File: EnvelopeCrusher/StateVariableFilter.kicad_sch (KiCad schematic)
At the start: 21 parts

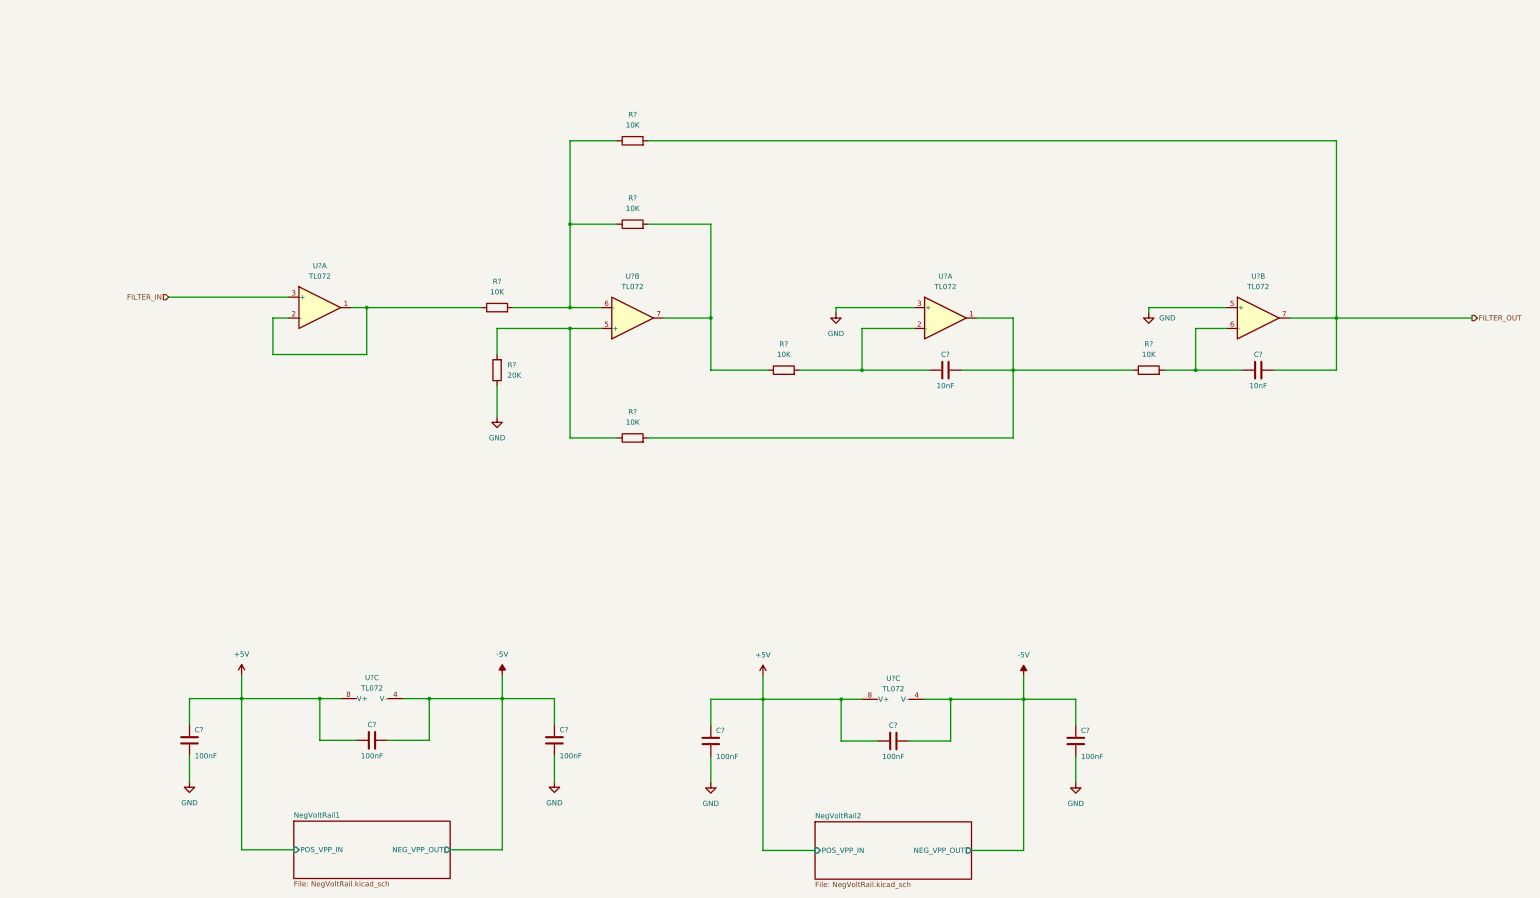
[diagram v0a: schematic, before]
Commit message: updated signal path
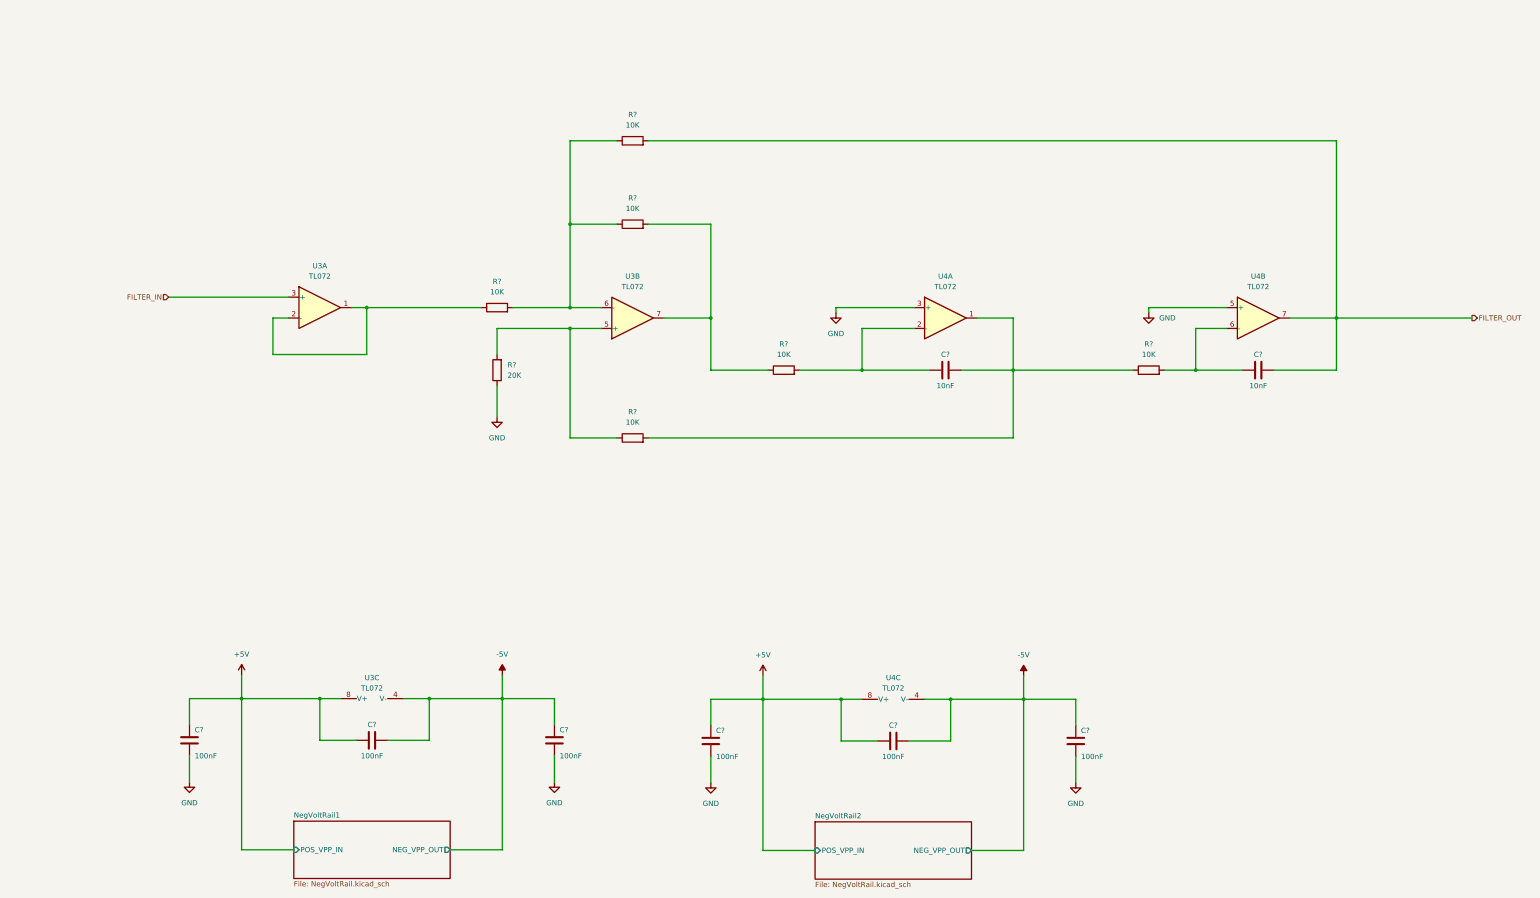
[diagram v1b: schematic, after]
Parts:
- gave numbers to parts that had none: 2
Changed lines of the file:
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@@
   (symbol (lib_id "Amplifier_Operational:TL072") (at 247.65 111.76 0) (unit 1)
     (in_bom yes) (on_board yes) (fields_autoplaced)
-    (property "Reference" "U?" (id 0) (at 247.65 101.6 0))
+    (property "Reference" "U4" (id 0) (at 247.65 101.6 0))
     (property "Value" "TL072" (id 1) (at 247.65 104.14 0))
     (property "Footprint" "" (id 2) (at 247.65 111.76 0)
@@
   (symbol (lib_id "Amplifier_Operational:TL072") (at 171.45 111.76 0) (mirror x) (unit 2)
     (in_bom yes) (on_board yes) (fields_autoplaced)
-    (property "Reference" "U?" (id 0) (at 171.45 101.6 0))
+    (property "Reference" "U3" (id 0) (at 171.45 101.6 0))
     (property "Value" "TL072" (id 1) (at 171.45 104.14 0))
     (property "Footprint" "" (id 2) (at 171.45 111.76 0)
@@
   (symbol (lib_id "Amplifier_Operational:TL072") (at 107.95 201.93 90) (unit 3)
     (in_bom yes) (on_board yes) (fields_autoplaced)
-    (property "Reference" "U?" (id 0) (at 107.95 199.39 90))
+    (property "Reference" "U3" (id 0) (at 107.95 199.39 90))
     (property "Value" "TL072" (id 1) (at 107.95 201.93 90))
     (property "Footprint" "" (id 2) (at 107.95 201.93 0)
@@
   (symbol (lib_id "Amplifier_Operational:TL072") (at 234.95 202.0941 90) (unit 3)
     (in_bom yes) (on_board yes) (fields_autoplaced)
-    (property "Reference" "U?" (id 0) (at 234.95 199.5541 90))
-    (property "Value" "TL072" (id 1) (at 234.95 202.0941 90))
+    (property "Reference" "U4" (id 0) (at 234.95 199.39 90))
+    (property "Value" "TL072" (id 1) (at 234.95 201.93 90))
     (property "Footprint" "" (id 2) (at 234.95 202.0941 0)
       (effects (font (size 1.27 1.27)) hide)
@@
   (symbol (lib_id "Amplifier_Operational:TL072") (at 95.25 109.22 0) (unit 1)
     (in_bom yes) (on_board yes) (fields_autoplaced)
-    (property "Reference" "U?" (id 0) (at 95.25 99.06 0))
+    (property "Reference" "U3" (id 0) (at 95.25 99.06 0))
     (property "Value" "TL072" (id 1) (at 95.25 101.6 0))
     (property "Footprint" "" (id 2) (at 95.25 109.22 0)
@@
   (symbol (lib_id "Amplifier_Operational:TL072") (at 323.85 111.76 0) (unit 2)
     (in_bom yes) (on_board yes) (fields_autoplaced)
-    (property "Reference" "U?" (id 0) (at 323.85 101.6 0))
+    (property "Reference" "U4" (id 0) (at 323.85 101.6 0))
     (property "Value" "TL072" (id 1) (at 323.85 104.14 0))
     (property "Footprint" "" (id 2) (at 323.85 111.76 0)

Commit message: Add routing
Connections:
- net SWEEP_3Y: now reaches C?.1, U4.2 (-)
- net SWEEP_3Y: no longer R?.2
- net SWEEP_4Y: now reaches C?.1, U4.6 (-)
- net SWEEP_4Y: no longer R?.2
- new net SWEEP_3Z: R?.2
- new net SWEEP_4Z: R?.2
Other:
- note added: "74HC4066 Analog Switch"
- moved on the sheet: C?, R?, U3A, U3B, U4A

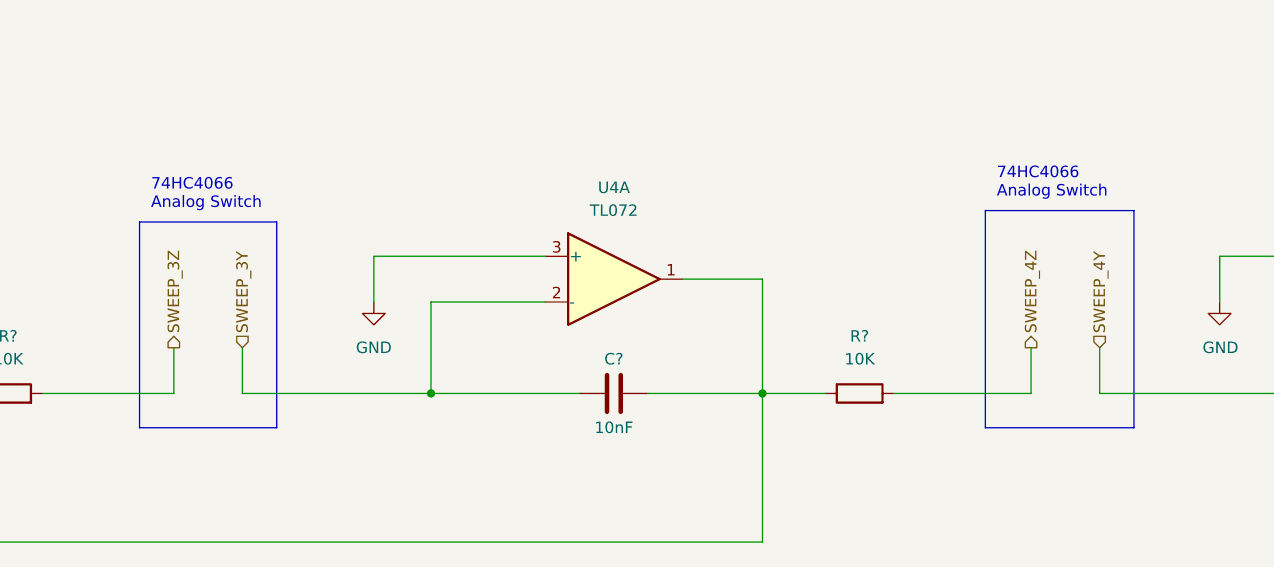
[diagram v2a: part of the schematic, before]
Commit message: REARRANGED BLOCK DIAGRAM AND ROUTING
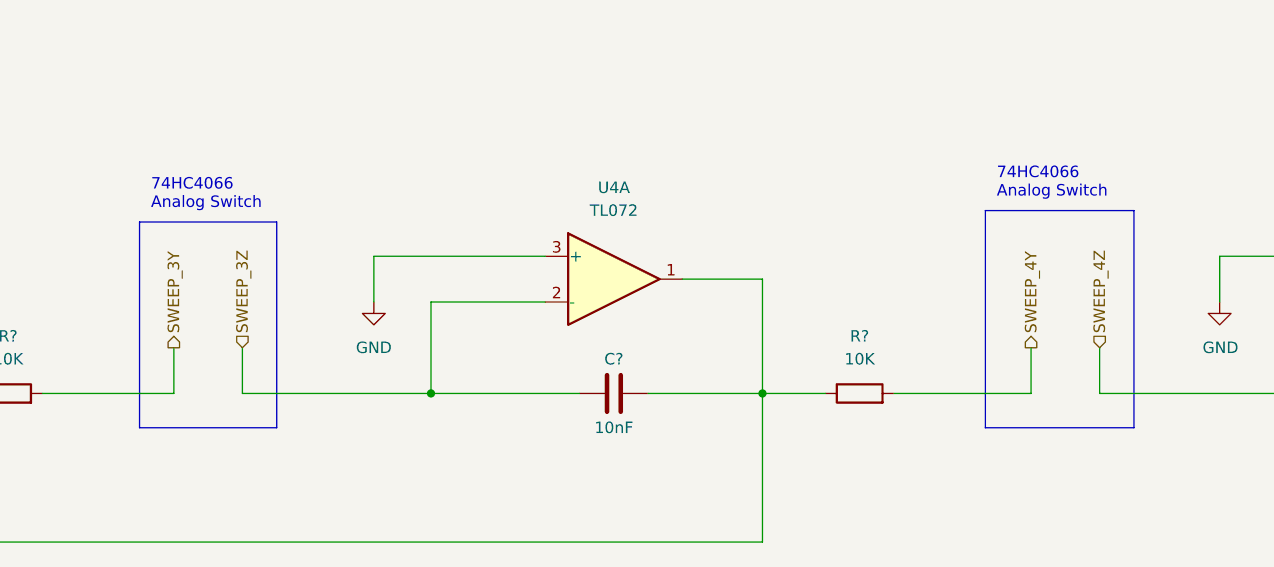
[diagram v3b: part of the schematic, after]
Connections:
- net SWEEP_3Y: now also R?.2; no longer C?.1, U4.2 (-)
- net SWEEP_3Z: now also C?.1, U4.2 (-); no longer R?.2
- net SWEEP_4Y: now also R?.2; no longer C?.1, U4.6 (-)
- net SWEEP_4Z: now also C?.1, U4.6 (-); no longer R?.2
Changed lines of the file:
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@@
     (effects (font (size 1.27 1.27)) (justify left))
   )
-  (hierarchical_label "SWEEP_4Z" (shape output) (at 279.4 119.38 90)
+  (hierarchical_label "SWEEP_4Z" (shape input) (at 287.02 119.38 90)
     (effects (font (size 1.27 1.27)) (justify left))
   )
-  (hierarchical_label "SWEEP_4Y" (shape input) (at 287.02 119.38 90)
+  (hierarchical_label "SWEEP_4Y" (shape output) (at 279.4 119.38 90)
     (effects (font (size 1.27 1.27)) (justify left))
   )
@@
     (effects (font (size 1.27 1.27)) (justify right))
   )
-  (hierarchical_label "SWEEP_3Y" (shape input) (at 191.77 119.38 90)
+  (hierarchical_label "SWEEP_3Y" (shape output) (at 184.15 119.38 90)
     (effects (font (size 1.27 1.27)) (justify left))
   )
-  (hierarchical_label "SWEEP_3Z" (shape output) (at 184.15 119.38 90)
+  (hierarchical_label "SWEEP_3Z" (shape input) (at 191.77 119.38 90)
     (effects (font (size 1.27 1.27)) (justify left))
   )

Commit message: Completed Schematic
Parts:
- gave numbers to parts that had none: 15
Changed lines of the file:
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@@
+    (stroke (width 0) (type default) (color 0 0 0 0))
+  )
+  (wire (pts (xy 121.92 198.12) (xy 121.92 204.47))
     (stroke (width 0) (type default) (color 0 0 0 0))
   )
@@
   (symbol (lib_id "power:GND") (at 300.355 114.3 0) (unit 1)
     (in_bom yes) (on_board yes)
-    (property "Reference" "#PWR?" (id 0) (at 300.355 120.65 0)
+    (property "Reference" "#PWR030" (id 0) (at 300.355 120.65 0)
       (effects (font (size 1.27 1.27)) hide)
     )
@@
   (symbol (lib_id "power:+5V") (at 76.2 198.7479 0) (unit 1)
     (in_bom yes) (on_board yes) (fields_autoplaced)
-    (property "Reference" "#PWR?" (id 0) (at 76.2 202.5579 0)
+    (property "Reference" "#PWR021" (id 0) (at 76.2 202.5579 0)
       (effects (font (size 1.27 1.27)) hide)
     )
@@
   (symbol (lib_id "Device:R") (at 104.14 109.22 90) (unit 1)
     (in_bom yes) (on_board yes) (fields_autoplaced)
-    (property "Reference" "R?" (id 0) (at 104.14 102.87 90))
+    (property "Reference" "R4" (id 0) (at 104.14 102.87 90))
     (property "Value" "10K" (id 1) (at 104.14 105.41 90))
     (property "Footprint" "Resistor_SMD:R_0805_2012Metric_Pad1.20x1.40mm_HandSolder" (id 2) (at 104.14 110.998 90)
@@
   (symbol (lib_id "Device:C") (at 152.4 214.63 180) (unit 1)
     (in_bom yes) (on_board yes)
-    (property "Reference" "C?" (id 0) (at 153.67 212.09 0)
+    (property "Reference" "C9" (id 0) (at 153.67 212.09 0)
       (effects (font (size 1.27 1.27)) (justify right))
     )
@@
   (symbol (lib_id "power:+5V") (at 203.2 198.912 0) (unit 1)
     (in_bom yes) (on_board yes) (fields_autoplaced)
-    (property "Reference" "#PWR?" (id 0) (at 203.2 202.722 0)
+    (property "Reference" "#PWR026" (id 0) (at 203.2 202.722 0)
       (effects (font (size 1.27 1.27)) hide)
     )
@@
   (symbol (lib_id "Device:C") (at 279.4 214.7941 180) (unit 1)
     (in_bom yes) (on_board yes)
-    (property "Reference" "C?" (id 0) (at 280.67 212.2541 0)
+    (property "Reference" "C13" (id 0) (at 280.67 212.2541 0)
       (effects (font (size 1.27 1.27)) (justify right))
     )
@@
   (symbol (lib_id "Device:C") (at 233.045 124.46 90) (unit 1)
     (in_bom yes) (on_board yes)
-    (property "Reference" "C?" (id 0) (at 233.045 120.65 90))
+    (property "Reference" "C11" (id 0) (at 233.045 120.65 90))
     (property "Value" "10nF" (id 1) (at 233.045 128.27 90))
     (property "Footprint" "Capacitor_SMD:C_0805_2012Metric_Pad1.18x1.45mm_HandSolder" (id 2) (at 236.855 123.4948 0)
@@
   (symbol (lib_id "power:GND") (at 104.14 135.89 0) (unit 1)
     (in_bom yes) (on_board yes) (fields_autoplaced)
-    (property "Reference" "#PWR?" (id 0) (at 104.14 142.24 0)
+    (property "Reference" "#PWR022" (id 0) (at 104.14 142.24 0)
       (effects (font (size 1.27 1.27)) hide)
     )
@@
   (symbol (lib_id "power:GND") (at 206.375 114.3 0) (unit 1)
     (in_bom yes) (on_board yes) (fields_autoplaced)
-    (property "Reference" "#PWR?" (id 0) (at 206.375 120.65 0)
+    (property "Reference" "#PWR027" (id 0) (at 206.375 120.65 0)
       (effects (font (size 1.27 1.27)) hide)
     )
@@
   (symbol (lib_id "Device:R") (at 104.14 124.46 180) (unit 1)
     (in_bom yes) (on_board yes) (fields_autoplaced)
-    (property "Reference" "R?" (id 0) (at 106.68 123.1899 0)
+    (property "Reference" "R5" (id 0) (at 106.68 123.1899 0)
       (effects (font (size 1.27 1.27)) (justify right))
     )
@@
   (symbol (lib_id "Device:R") (at 260.35 124.46 90) (unit 1)
     (in_bom yes) (on_board yes) (fields_autoplaced)
-    (property "Reference" "R?" (id 0) (at 260.35 118.11 90))
+    (property "Reference" "R11" (id 0) (at 260.35 118.11 90))
     (property "Value" "10K" (id 1) (at 260.35 120.65 90))
     (property "Footprint" "Resistor_SMD:R_0805_2012Metric_Pad1.20x1.40mm_HandSolder" (id 2) (at 260.35 126.238 90)
@@
   (symbol (lib_id "Device:R") (at 165.735 124.46 90) (unit 1)
     (in_bom yes) (on_board yes) (fields_autoplaced)
-    (property "Reference" "R?" (id 0) (at 165.735 118.11 90))
+    (property "Reference" "R10" (id 0) (at 165.735 118.11 90))
     (property "Value" "10K" (id 1) (at 165.735 120.65 90))
     (property "Footprint" "Resistor_SMD:R_0805_2012Metric_Pad1.20x1.40mm_HandSolder" (id 2) (at 165.735 126.238 90)
@@
   (symbol (lib_id "Device:C") (at 323.85 124.46 90) (unit 1)
     (in_bom yes) (on_board yes)
-    (property "Reference" "C?" (id 0) (at 323.85 120.65 90))
+    (property "Reference" "C14" (id 0) (at 323.85 120.65 90))
     (property "Value" "10nF" (id 1) (at 323.85 128.27 90))
     (property "Footprint" "Capacitor_SMD:C_0805_2012Metric_Pad1.18x1.45mm_HandSolder" (id 2) (at 327.66 123.4948 0)
@@
   (symbol (lib_id "Device:R") (at 137.16 88.9 90) (unit 1)
     (in_bom yes) (on_board yes) (fields_autoplaced)
-    (property "Reference" "R?" (id 0) (at 137.16 82.55 90))
+    (property "Reference" "R8" (id 0) (at 137.16 82.55 90))
     (property "Value" "10K" (id 1) (at 137.16 85.09 90))
     (property "Footprint" "Resistor_SMD:R_0805_2012Metric_Pad1.20x1.40mm_HandSolder" (id 2) (at 137.16 90.678 90)
@@
     (pin "2")
   )
+  (symbol (lib_id "power:PWR_FLAG") (at 121.92 198.12 0) (unit 1)
+    (in_bom yes) (on_board yes) (fields_autoplaced)
+    (property "Reference" "#FLG?" (id 0) (at 121.92 196.215 0)
+      (effects (font (size 1.27 1.27)) hide)
+    )
+    (property "Value" "PWR_FLAG" (id 1) (at 121.92 193.04 0))
+    (property "Footprint" "" (id 2) (at 121.92 198.12 0)
+      (effects (font (size 1.27 1.27)) hide)
+    )
+    (property "Datasheet" "~" (id 3) (at 121.92 198.12 0)
+      (effects (font (size 1.27 1.27)) hide)
+    )
+    (pin "1")
+  )
   (symbol (lib_id "power:GND") (at 63.5 224.79 0) (unit 1)
     (in_bom yes) (on_board yes) (fields_autoplaced)
-    (property "Reference" "#PWR?" (id 0) (at 63.5 231.14 0)
+    (property "Reference" "#PWR020" (id 0) (at 63.5 231.14 0)
       (effects (font (size 1.27 1.27)) hide)
     )
@@
   (symbol (lib_id "Device:C") (at 190.5 214.7941 180) (unit 1)
     (in_bom yes) (on_board yes)
-    (property "Reference" "C?" (id 0) (at 191.77 212.2541 0)
+    (property "Reference" "C10" (id 0) (at 191.77 212.2541 0)
       (effects (font (size 1.27 1.27)) (justify right))
     )
@@
   (symbol (lib_id "Device:R") (at 137.16 68.58 90) (unit 1)
     (in_bom yes) (on_board yes) (fields_autoplaced)
-    (property "Reference" "R?" (id 0) (at 137.16 62.23 90))
+    (property "Reference" "R7" (id 0) (at 137.16 62.23 90))
     (property "Value" "10K" (id 1) (at 137.16 64.77 90))
     (property "Footprint" "Resistor_SMD:R_0805_2012Metric_Pad1.20x1.40mm_HandSolder" (id 2) (at 137.16 70.358 90)
@@
   (symbol (lib_id "power:GND") (at 190.5 224.9541 0) (unit 1)
     (in_bom yes) (on_board yes) (fields_autoplaced)
-    (property "Reference" "#PWR?" (id 0) (at 190.5 231.3041 0)
+    (property "Reference" "#PWR025" (id 0) (at 190.5 231.3041 0)
       (effects (font (size 1.27 1.27)) hide)
     )
@@
   (symbol (lib_id "Device:R") (at 137.16 140.97 90) (unit 1)
     (in_bom yes) (on_board yes) (fields_autoplaced)
-    (property "Reference" "R?" (id 0) (at 137.16 134.62 90))
+    (property "Reference" "R9" (id 0) (at 137.16 134.62 90))
     (property "Value" "10K" (id 1) (at 137.16 137.16 90))
     (property "Footprint" "Resistor_SMD:R_0805_2012Metric_Pad1.20x1.40mm_HandSolder" (id 2) (at 137.16 142.748 90)
@@
   (symbol (lib_id "Device:C") (at 107.95 214.63 90) (unit 1)
     (in_bom yes) (on_board yes)
-    (property "Reference" "C?" (id 0) (at 107.95 210.82 90))
+    (property "Reference" "C8" (id 0) (at 107.95 210.82 90))
     (property "Value" "100nF" (id 1) (at 107.95 218.44 90))
     (property "Footprint" "Capacitor_SMD:C_0805_2012Metric_Pad1.18x1.45mm_HandSolder" (id 2) (at 111.76 213.6648 0)
@@
   (symbol (lib_id "power:GND") (at 279.4 224.9541 0) (unit 1)
     (in_bom yes) (on_board yes) (fields_autoplaced)
-    (property "Reference" "#PWR?" (id 0) (at 279.4 231.3041 0)
+    (property "Reference" "#PWR029" (id 0) (at 279.4 231.3041 0)
       (effects (font (size 1.27 1.27)) hide)
     )
@@
   (symbol (lib_id "power:-5V") (at 266.7 198.912 0) (unit 1)
     (in_bom yes) (on_board yes) (fields_autoplaced)
-    (property "Reference" "#PWR?" (id 0) (at 266.7 196.372 0)
+    (property "Reference" "#PWR028" (id 0) (at 266.7 196.372 0)
       (effects (font (size 1.27 1.27)) hide)
     )
@@
   (symbol (lib_id "Device:C") (at 234.95 214.7941 90) (unit 1)
     (in_bom yes) (on_board yes)
-    (property "Reference" "C?" (id 0) (at 234.95 210.9841 90))
+    (property "Reference" "C12" (id 0) (at 234.95 210.9841 90))
     (property "Value" "100nF" (id 1) (at 234.95 218.6041 90))
     (property "Footprint" "Capacitor_SMD:C_0805_2012Metric_Pad1.18x1.45mm_HandSolder" (id 2) (at 238.76 213.8289 0)
@@
   (symbol (lib_id "power:-5V") (at 139.7 198.7479 0) (unit 1)
     (in_bom yes) (on_board yes) (fields_autoplaced)
-    (property "Reference" "#PWR?" (id 0) (at 139.7 196.2079 0)
+    (property "Reference" "#PWR023" (id 0) (at 139.7 196.2079 0)
       (effects (font (size 1.27 1.27)) hide)
     )
@@
   (symbol (lib_id "power:GND") (at 152.4 224.79 0) (unit 1)
     (in_bom yes) (on_board yes) (fields_autoplaced)
-    (property "Reference" "#PWR?" (id 0) (at 152.4 231.14 0)
+    (property "Reference" "#PWR024" (id 0) (at 152.4 231.14 0)
       (effects (font (size 1.27 1.27)) hide)
     )
@@
   (symbol (lib_id "Device:C") (at 63.5 214.63 180) (unit 1)
     (in_bom yes) (on_board yes)
-    (property "Reference" "C?" (id 0) (at 64.77 212.09 0)
-      (effects (font (size 1.27 1.27)) (justify right))
-    )
+    (property "Reference" "C7" (id 0) (at 64.77 212.09 0)
+      (effects (font (size 1.27 1.27)) (justify right))
+    )
